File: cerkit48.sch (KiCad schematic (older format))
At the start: 104 parts, among them J1 I2C, SW1 SW_Push_Dual_x2, SW10 CherryMX, SW11 CherryMX, SW12 CherryMX, SW13 CherryMX, SW14 CherryMX, SW15 CherryMX, SW16 CherryMX, SW17 CherryMX, SW18 CherryMX, SW19 CherryMX, SW2 CherryMX, SW20 CherryMX, SW21 CherryMX, SW22 CherryMX, SW23 CherryMX, SW24 CherryMX, SW25 CherryMX, SW26 CherryMX, SW27 CherryMX, SW28 CherryMX, SW29 CherryMX, SW3 CherryMX, SW30 CherryMX, SW31 CherryMX, SW32 CherryMX, SW33 CherryMX, SW34 CherryMX, SW35 CherryMX, SW36 CherryMX, SW37 CherryMX, SW38 CherryMX, SW39 CherryMX, SW4 CherryMX, SW40 CherryMX, SW41 CherryMX, SW42 CherryMX, SW43 CherryMX, SW44 CherryMX, SW45 CherryMX, SW46 CherryMX, SW47 CherryMX, SW48 CherryMX, SW49 CherryMX, SW5 CherryMX, SW6 CherryMX, SW7 CherryMX, SW8 CherryMX, SW9 CherryMX, U1 proton_c

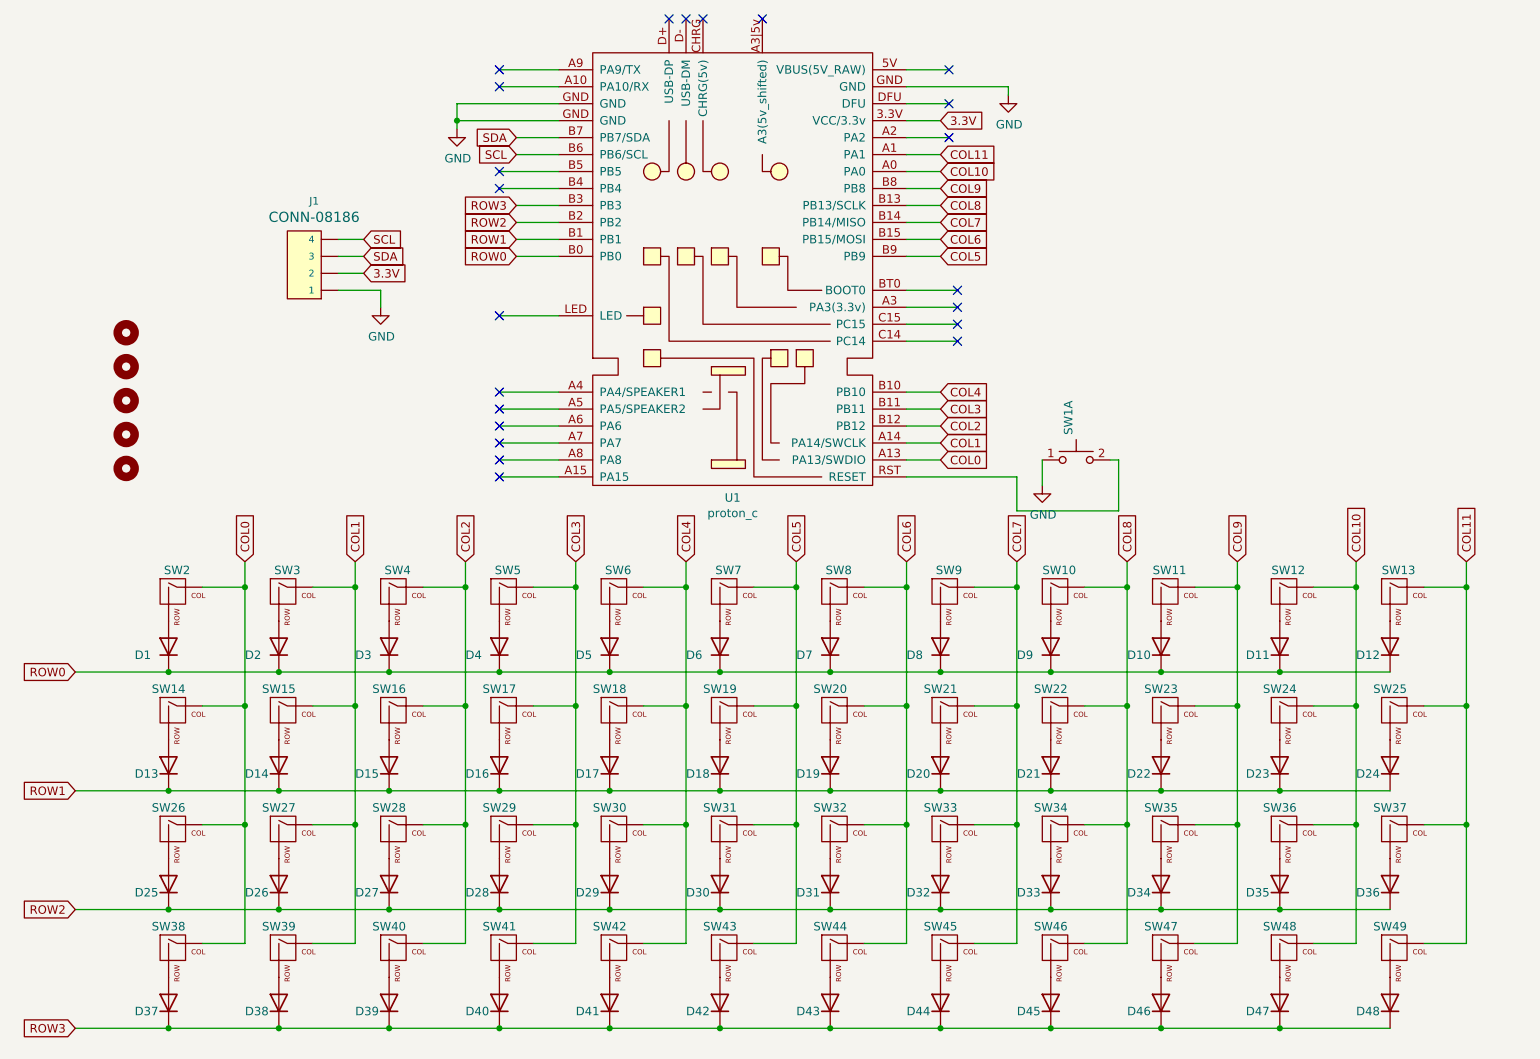
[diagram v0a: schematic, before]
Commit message: reworked back traces
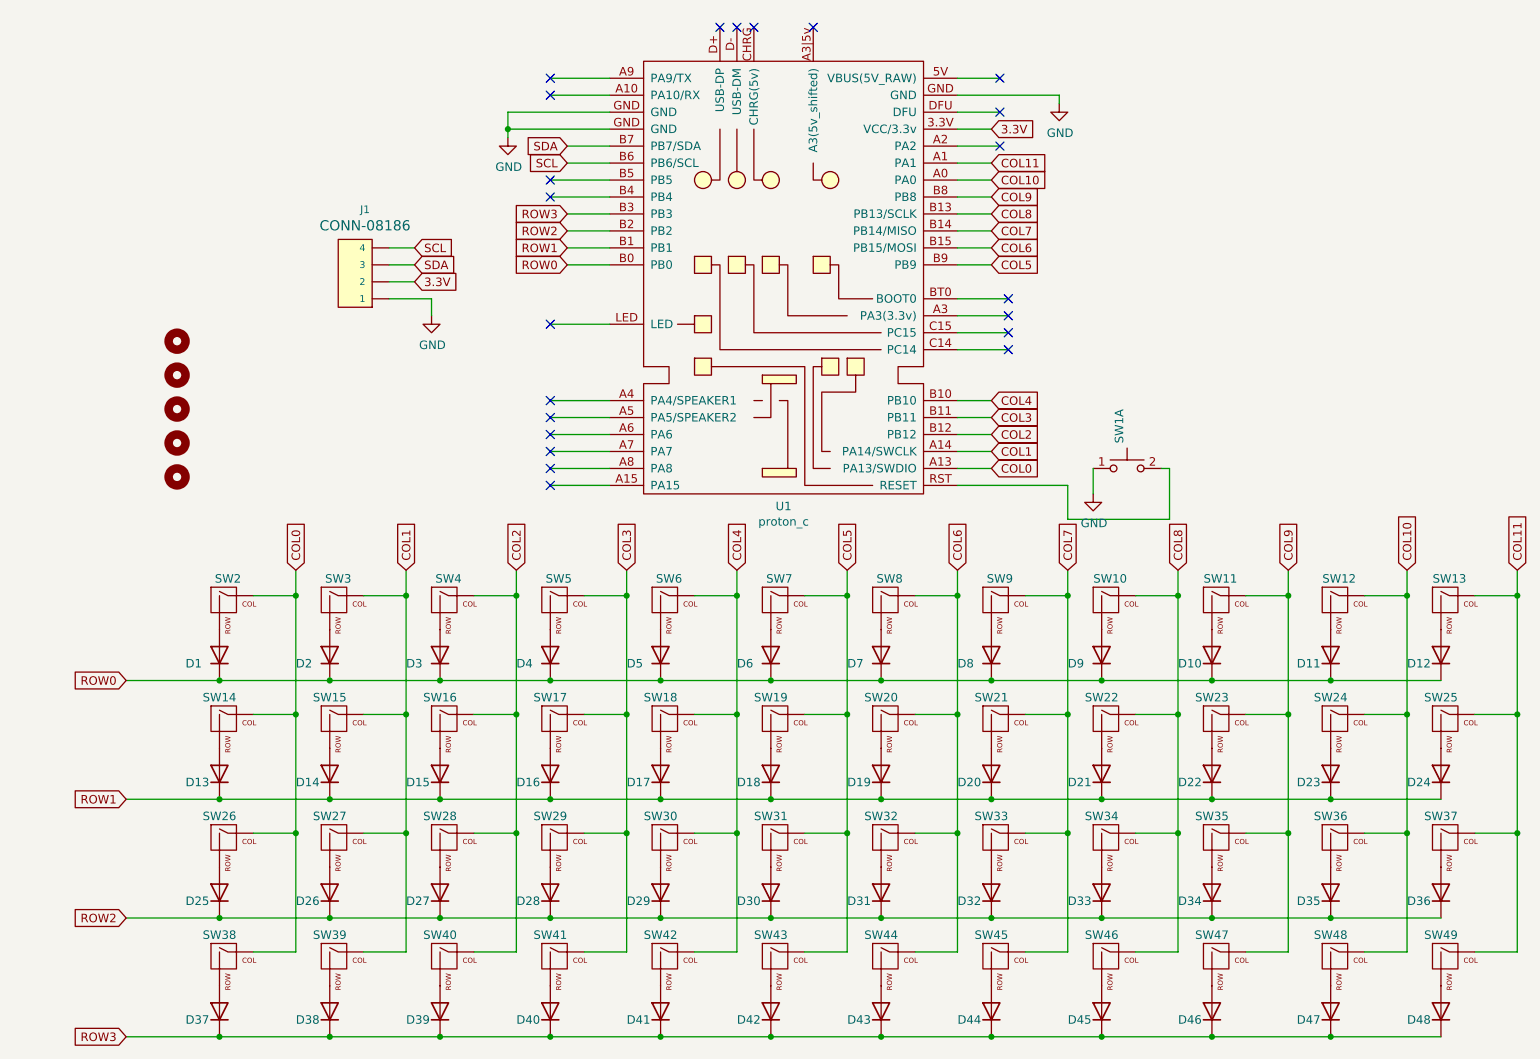
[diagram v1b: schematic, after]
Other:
- moved on the sheet: D1, D10, D11, D12, D13, D14, D15, D16, D17, D18, D19, D2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

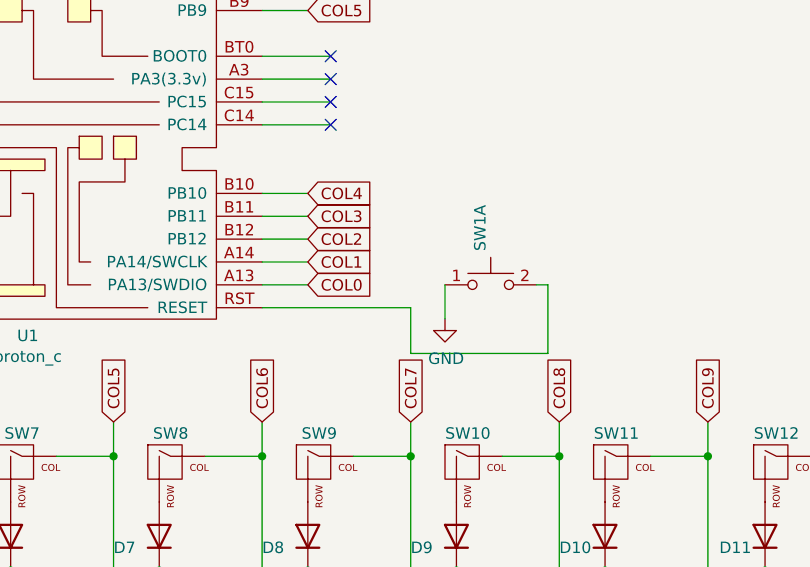
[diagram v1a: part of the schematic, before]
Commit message: reworked diodes so the board could be smaller
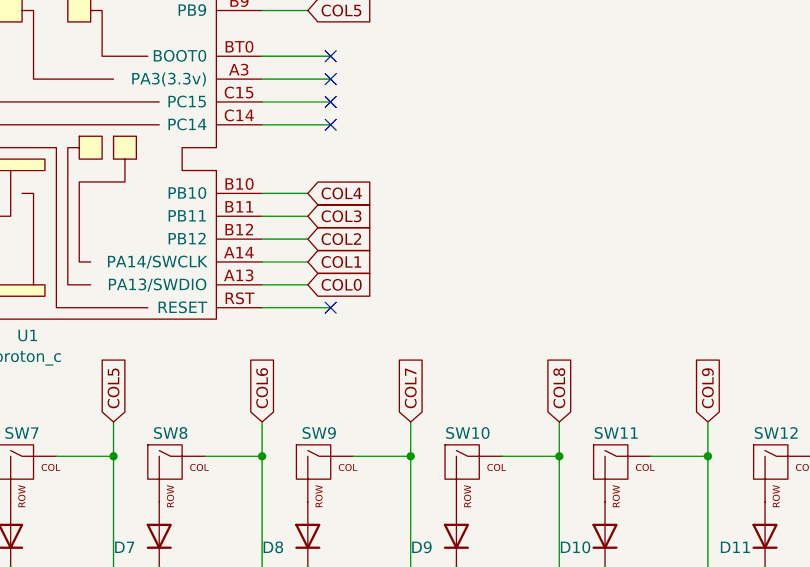
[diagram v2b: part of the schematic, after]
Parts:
- removed SW1: SW_Push_Dual_x2, Button_Switch_THT:SW_PUSH_6mm, symbol Switch:SW_Push_Dual_x2
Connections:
- no-connect marks 22 -> 23
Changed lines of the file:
@@
 Text GLabel 6300 1350 2    50   Input ~ 0
 COL11
-$Comp
-L Switch:SW_Push_Dual_x2 SW1
-U 1 1 5EF562D3
-P 7100 3150
-F 0 "SW1" V 7054 3298 50  0000 L CNN
-F 1 "SW_Push_Dual_x2" V 7145 3298 50  0001 L CNN
-F 2 "Button_Switch_THT:SW_PUSH_6mm" H 7100 3350 50  0001 C CNN
-F 3 "~" H 7100 3350 50  0001 C CNN
-	1    7100 3150
-	1    0    0    -1
-$EndComp
-Wire Wire Line
-	6100 3250 6750 3250
-Wire Wire Line
-	6750 3250 6750 3450
-Wire Wire Line
-	6750 3450 7350 3450
 Wire Wire Line
 	6100 3150 6300 3150
@@
 	6350 850  6100 850
 $Comp
-L power:GND #PWR04
-U 1 1 5ED38B7A
-P 6900 3300
-F 0 "#PWR04" H 6900 3050 50  0001 C CNN
-F 1 "GND" H 6905 3127 50  0000 C CNN
-F 2 "" H 6900 3300 50  0001 C CNN
-F 3 "" H 6900 3300 50  0001 C CNN
-	1    6900 3300
-	1    0    0    -1
-$EndComp
-Wire Wire Line
-	7350 3450 7350 3150
-Wire Wire Line
-	7350 3150 7300 3150
-Wire Wire Line
-	6900 3150 6900 3300
-$Comp
 L power:GND #PWR02
 U 1 1 5ED57742
@@
 	6750 6000 6500 6000
 Connection ~ 6750 5300
-Wire Wire Line
-	7400 3750 7400 3900
 $Comp
 L MX_Alps_Hybrid:MX-NoLED SW10
@@
 	0    -1   -1   0
 $EndComp
-Text GLabel 7400 3750 1    50   Input ~ 0
-COL8
 $Comp
 L MX_Alps_Hybrid:MX-NoLED SW22
@@
 $EndComp
 Wire Wire Line
-	7150 3900 7400 3900
-Connection ~ 7400 3900
-Wire Wire Line
-	7400 3900 7400 4600
-Wire Wire Line
 	7150 4600 7400 4600
 Connection ~ 7400 4600
@@
 	8300 6500 8950 6500
 Connection ~ 8300 6500
+NoConn ~ 6400 3250
+Wire Wire Line
+	6400 3250 6100 3250
+Wire Wire Line
+	7400 3750 7400 3900
+Text GLabel 7400 3750 1    50   Input ~ 0
+COL8
+Wire Wire Line
+	7150 3900 7400 3900
+Connection ~ 7400 3900
+Wire Wire Line
+	7400 3900 7400 4600
 $EndSCHEMATC

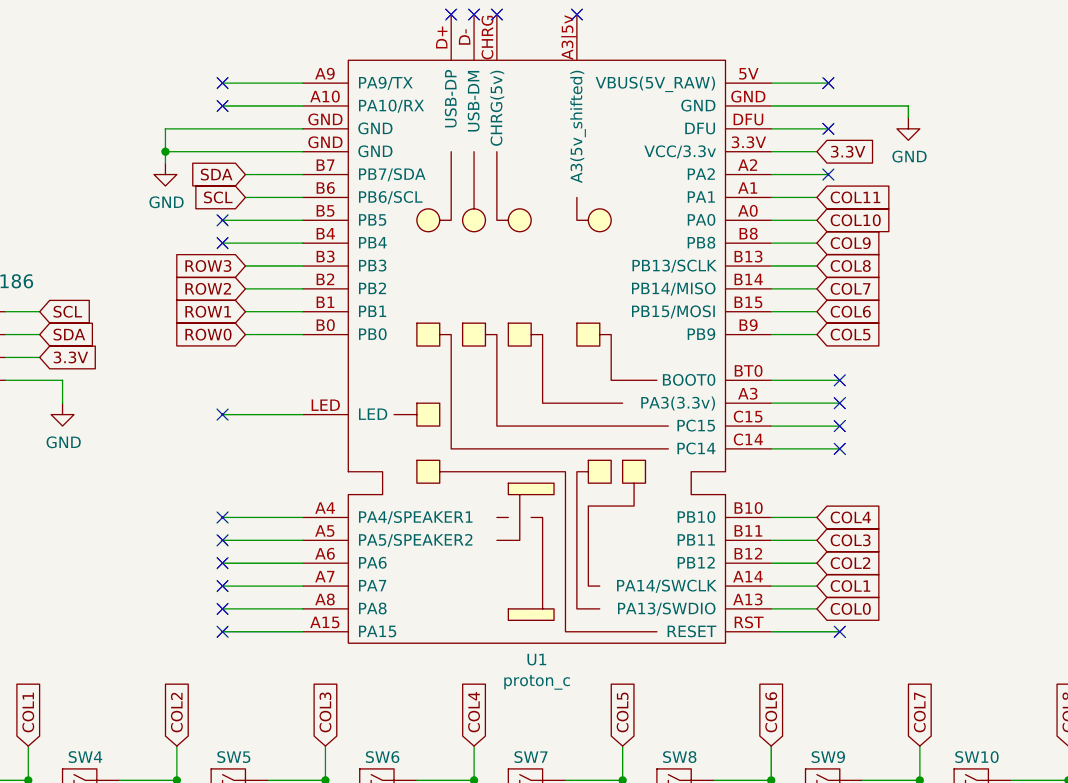
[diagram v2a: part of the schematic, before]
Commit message: Move Proton to bottom of board and made board smaller
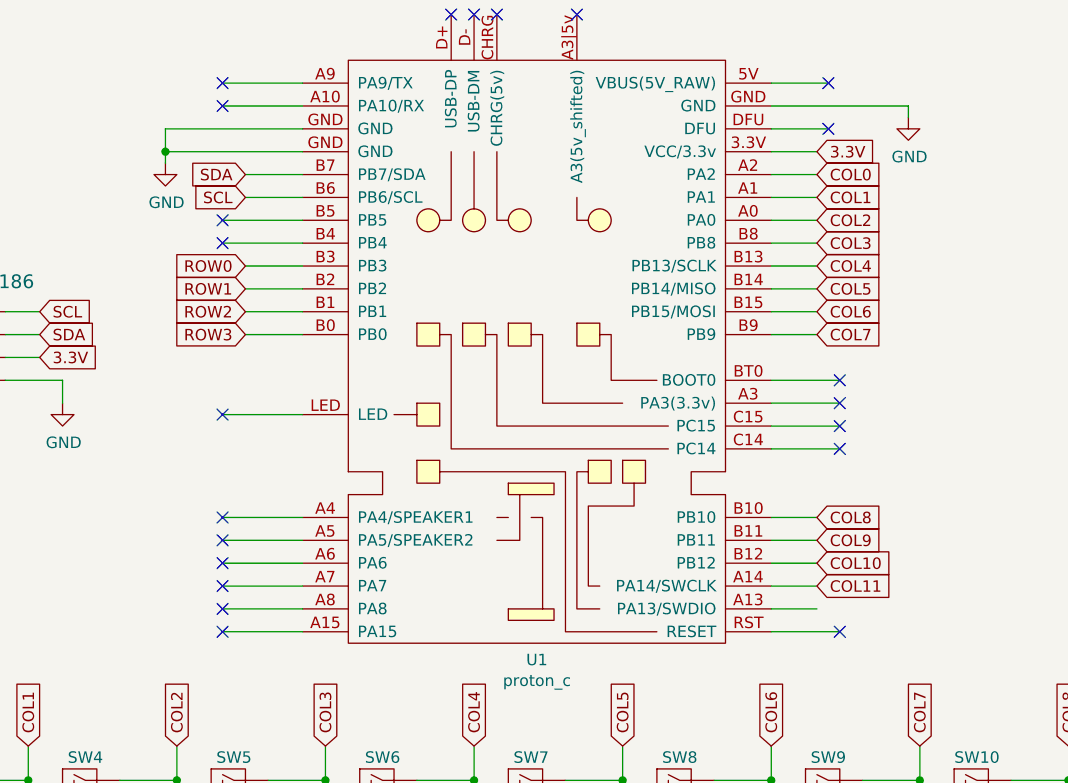
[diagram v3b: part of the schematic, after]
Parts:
- U1: footprint proton_c:proton_c -> cerkit48:proton_c_no_center_pins
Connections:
- net COL0: now also U1.A2 (PA2); no longer U1.A13 (PA13/SWDIO)
- net COL1: now also U1.A1 (PA1); no longer U1.A14 (PA14/SWCLK)
- net COL10: now also U1.B12 (PB12); no longer U1.A0 (PA0)
- net COL11: now also U1.A14 (PA14/SWCLK); no longer U1.A1 (PA1)
- net COL2: now also U1.A0 (PA0); no longer U1.B12 (PB12)
- net COL3: now also U1.B8 (PB8); no longer U1.B11 (PB11)
- net COL4: now also U1.B13 (PB13/SCLK); no longer U1.B10 (PB10)
- net COL5: now also U1.B14 (PB14/MISO); no longer U1.B9 (PB9)
- net COL7: now also U1.B9 (PB9); no longer U1.B14 (PB14/MISO)
- net COL8: now also U1.B10 (PB10); no longer U1.B13 (PB13/SCLK)
- net COL9: now also U1.B11 (PB11); no longer U1.B8 (PB8)
- net ROW0: now also U1.B3 (PB3); no longer U1.B0 (PB0)
- net ROW1: now also U1.B2 (PB2); no longer U1.B1 (PB1)
- net ROW2: now also U1.B1 (PB1); no longer U1.B2 (PB2)
- net ROW3: now also U1.B0 (PB0); no longer U1.B3 (PB3)
- no-connect marks 23 -> 22
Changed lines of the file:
@@
 F 0 "U1" H 5075 327 50  0000 C CNN
 F 1 "proton_c" H 5075 236 50  0000 C CNN
-F 2 "proton_c:proton_c" H 4950 1850 50  0001 C CNN
+F 2 "cerkit48:proton_c_no_center_pins" H 4950 1850 50  0001 C CNN
 F 3 "" H 4950 1850 50  0001 C CNN
 	1    5100 1850
 	1    0    0    -1
 $EndComp
+Text GLabel 3800 1650 0    50   Input ~ 0
+ROW0
+Text GLabel 3800 1750 0    50   Input ~ 0
+ROW1
+Text GLabel 3800 1850 0    50   Input ~ 0
+ROW2
 Text GLabel 3800 1950 0    50   Input ~ 0
-ROW0
-Text GLabel 3800 1850 0    50   Input ~ 0
-ROW1
-Text GLabel 3800 1750 0    50   Input ~ 0
-ROW2
-Text GLabel 3800 1650 0    50   Input ~ 0
 ROW3
-Text GLabel 6300 3150 2    50   Input ~ 0
-COL0
-Text GLabel 6300 3050 2    50   Input ~ 0
+Text GLabel 6300 1350 2    50   Input ~ 0
 COL1
-Text GLabel 6300 2950 2    50   Input ~ 0
+Text GLabel 6300 1450 2    50   Input ~ 0
 COL2
-Text GLabel 6300 2850 2    50   Input ~ 0
+Text GLabel 6300 1550 2    50   Input ~ 0
 COL3
-Text GLabel 6300 2750 2    50   Input ~ 0
+Text GLabel 6300 1650 2    50   Input ~ 0
 COL4
-Text GLabel 6300 1950 2    50   Input ~ 0
+Text GLabel 6300 1750 2    50   Input ~ 0
 COL5
 Text GLabel 6300 1850 2    50   Input ~ 0
 COL6
-Text GLabel 6300 1750 2    50   Input ~ 0
+Text GLabel 6300 1950 2    50   Input ~ 0
 COL7
-Text GLabel 6300 1650 2    50   Input ~ 0
+Text GLabel 6300 2750 2    50   Input ~ 0
 COL8
-Text GLabel 6300 1550 2    50   Input ~ 0
+Text GLabel 6300 2850 2    50   Input ~ 0
 COL9
-Text GLabel 6300 1450 2    50   Input ~ 0
+Text GLabel 6300 2950 2    50   Input ~ 0
 COL10
-Text GLabel 6300 1350 2    50   Input ~ 0
+Text GLabel 6300 3050 2    50   Input ~ 0
 COL11
 Wire Wire Line
@@
 NoConn ~ 6350 850
 NoConn ~ 6350 1050
-NoConn ~ 6350 1250
 Wire Wire Line
 	3700 2300 4050 2300
@@
 Wire Wire Line
 	3700 3250 4050 3250
-Wire Wire Line
-	6350 1250 6100 1250
 Wire Wire Line
 	6350 1050 6100 1050
@@
 Wire Wire Line
 	7400 3900 7400 4600
+Text GLabel 6300 1250 2    50   Input ~ 0
+COL0
+Wire Wire Line
+	6300 1250 6100 1250
 $EndSCHEMATC

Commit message: flipped Proton so it will be arranged correctly on the back of the board.
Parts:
- J1: symbol SparkFun-Connectors:CONN_04POLAR -> Connector:Conn_01x04_Male
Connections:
- wire segments 193 -> 190
- no-connect marks 22 -> 16
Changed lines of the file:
@@
 	1    0    0    -1
 $EndComp
+Text GLabel 6300 1650 2    50   Input ~ 0
+ROW0
+Text GLabel 6300 1750 2    50   Input ~ 0
+ROW1
+Text GLabel 6300 1850 2    50   Input ~ 0
+ROW2
+Text GLabel 6300 2750 2    50   Input ~ 0
+ROW3
+Text GLabel 3800 1350 0    50   Input ~ 0
+COL1
+Text GLabel 3800 1450 0    50   Input ~ 0
+COL2
+Text GLabel 3800 1550 0    50   Input ~ 0
+COL3
 Text GLabel 3800 1650 0    50   Input ~ 0
-ROW0
+COL4
 Text GLabel 3800 1750 0    50   Input ~ 0
-ROW1
+COL5
 Text GLabel 3800 1850 0    50   Input ~ 0
-ROW2
-Text GLabel 3800 1950 0    50   Input ~ 0
-ROW3
-Text GLabel 6300 1350 2    50   Input ~ 0
-COL1
-Text GLabel 6300 1450 2    50   Input ~ 0
-COL2
-Text GLabel 6300 1550 2    50   Input ~ 0
-COL3
-Text GLabel 6300 1650 2    50   Input ~ 0
-COL4
-Text GLabel 6300 1750 2    50   Input ~ 0
-COL5
-Text GLabel 6300 1850 2    50   Input ~ 0
 COL6
-Text GLabel 6300 1950 2    50   Input ~ 0
-COL7
-Text GLabel 6300 2750 2    50   Input ~ 0
+Text GLabel 3700 2950 0    50   Input ~ 0
 COL8
-Text GLabel 6300 2850 2    50   Input ~ 0
+Text GLabel 3700 3050 0    50   Input ~ 0
 COL9
-Text GLabel 6300 2950 2    50   Input ~ 0
+Text GLabel 3700 3150 0    50   Input ~ 0
 COL10
-Text GLabel 6300 3050 2    50   Input ~ 0
+Text GLabel 3700 3250 0    50   Input ~ 0
 COL11
 Wire Wire Line
@@
 Wire Wire Line
 	6100 1350 6300 1350
-Text GLabel 2900 2050 2    50   Input ~ 0
+Text GLabel 2900 1500 0    50   Input ~ 0
 3.3V
 Text GLabel 6300 1150 2    50   Input ~ 0
@@
 NoConn ~ 3700 2750
 NoConn ~ 3700 2850
-NoConn ~ 3700 2950
-NoConn ~ 3700 3050
-NoConn ~ 3700 3150
-NoConn ~ 3700 3250
 NoConn ~ 3700 2300
-NoConn ~ 3700 1550
-NoConn ~ 3700 1450
-Text GLabel 2900 1850 2    50   Input ~ 0
+Text GLabel 2900 1300 0    50   Input ~ 0
 SCL
-Text GLabel 2900 1950 2    50   Input ~ 0
+Text GLabel 2900 1400 0    50   Input ~ 0
 SDA
-Wire Wire Line
-	3700 1450 4050 1450
-Wire Wire Line
-	3700 1550 4050 1550
 NoConn ~ 3700 950
 NoConn ~ 3700 850
-Text GLabel 3800 1250 0    50   Input ~ 0
+Text GLabel 6300 1950 2    50   Input ~ 0
 SDA
-Text GLabel 3800 1350 0    50   Input ~ 0
+Text GLabel 6300 1550 2    50   Input ~ 0
 SCL
 Wire Wire Line
@@
 Wire Wire Line
 	3700 2850 4050 2850
-Wire Wire Line
-	3700 2950 4050 2950
-Wire Wire Line
-	3700 3050 4050 3050
-Wire Wire Line
-	3700 3150 4050 3150
-Wire Wire Line
-	3700 3250 4050 3250
 Wire Wire Line
 	6350 1050 6100 1050
@@
 L power:GND #PWR03
 U 1 1 5ED88422
-P 3000 2250
-F 0 "#PWR03" H 3000 2000 50  0001 C CNN
-F 1 "GND" H 3005 2077 50  0000 C CNN
-F 2 "" H 3000 2250 50  0001 C CNN
-F 3 "" H 3000 2250 50  0001 C CNN
-	1    3000 2250
-	1    0    0    -1
-$EndComp
-Wire Wire Line
-	3000 2150 3000 2250
+P 2750 1750
+F 0 "#PWR03" H 2750 1500 50  0001 C CNN
+F 1 "GND" H 2755 1577 50  0000 C CNN
+F 2 "" H 2750 1750 50  0001 C CNN
+F 3 "" H 2750 1750 50  0001 C CNN
+	1    2750 1750
+	1    0    0    -1
+$EndComp
 Wire Wire Line
 	6400 2150 6100 2150
@@
 NoConn ~ 6400 2150
 $Comp
-L SparkFun-Connectors:CONN_04POLAR J1
+L Connector:Conn_01x04_Male J1
 U 1 1 5EF1EDAE
-P 2650 2150
-F 0 "J1" H 2608 2676 45  0000 C CNN
-F 1 "I2C" H 2608 2676 45  0001 C CNN
-F 2 "cerkit48:PIN_HEADER_I2C" H 2650 2650 20  0001 C CNN
-F 3 "" H 2650 2150 50  0001 C CNN
-F 4 "CONN-08186" H 2608 2581 60  0000 C CNN "Field4"
-	1    2650 2150
-	1    0    0    -1
-$EndComp
-Wire Wire Line
-	2900 1850 2750 1850
-Wire Wire Line
-	2750 1950 2900 1950
-Wire Wire Line
-	2750 2050 2900 2050
-Wire Wire Line
-	2750 2150 3000 2150
+P 3100 1500
+F 0 "J1" H 3250 1050 45  0000 C CNN
+F 1 "I2C" H 3058 2026 45  0001 C CNN
+F 2 "cerkit48:PIN_HEADER_I2C" H 3100 2000 20  0001 C CNN
+F 3 "" H 3100 1500 50  0001 C CNN
+F 4 "CONN-08186" H 3300 1200 60  0000 C CNN "Field4"
+	1    3100 1500
+	-1   0    0    1
+$EndComp
 $Comp
 L Mechanical:MountingHole H1
@@
 Wire Wire Line
 	7400 3900 7400 4600
-Text GLabel 6300 1250 2    50   Input ~ 0
+Text GLabel 3800 1250 0    50   Input ~ 0
 COL0
 Wire Wire Line
 	6300 1250 6100 1250
+Text GLabel 3800 1950 0    50   Input ~ 0
+COL7
+Wire Wire Line
+	3700 3250 4050 3250
+Wire Wire Line
+	3700 3150 4050 3150
+Wire Wire Line
+	3700 3050 4050 3050
+Wire Wire Line
+	3700 2950 4050 2950
+Wire Wire Line
+	3800 1450 4050 1450
+Wire Wire Line
+	3800 1550 4050 1550
+Wire Wire Line
+	2900 1600 2750 1600
+Wire Wire Line
+	2750 1600 2750 1750
 $EndSCHEMATC

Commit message: reset switch number annotations
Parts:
- renumbered SW2 to SW1, SW11 to SW10, SW12 to SW11, SW13 to SW12, SW14 to SW13, SW15 to SW14, SW16 to SW15, SW17 to SW16, SW18 to SW17, SW19 to SW18, SW20 to SW19, SW3 to SW2, SW21 to SW20, SW22 to SW21, SW23 to SW22, SW24 to SW23, SW25 to SW24, SW26 to SW25, SW27 to SW26, SW28 to SW27, SW29 to SW28, SW30 to SW29, SW4 to SW3, SW31 to SW30, SW32 to SW31, SW33 to SW32, SW34 to SW33, SW35 to SW34, SW36 to SW35, SW37 to SW36, SW38 to SW37, SW39 to SW38, SW40 to SW39, SW5 to SW4, SW41 to SW40, SW42 to SW41, SW43 to SW42, SW44 to SW43, SW45 to SW44, SW46 to SW45, SW47 to SW46, SW48 to SW47, SW49 to SW48, SW6 to SW5, SW7 to SW6, SW8 to SW7, SW9 to SW8, SW10 to SW9
